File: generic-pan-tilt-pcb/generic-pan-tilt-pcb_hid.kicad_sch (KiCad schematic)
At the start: 9 parts, among them SW3 219-12LPST, U5 MCP23017_SO

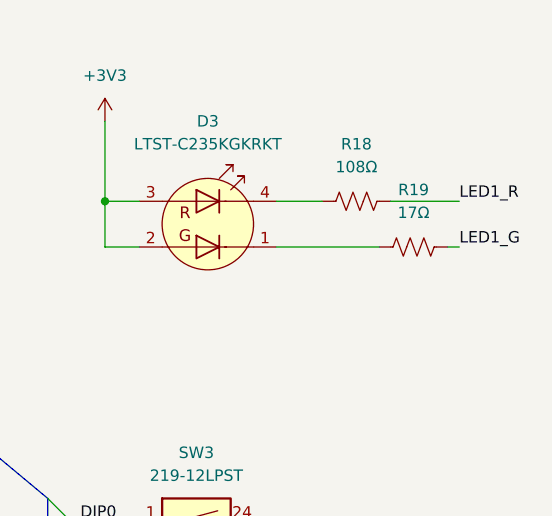
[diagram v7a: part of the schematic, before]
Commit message: fix LED resistors
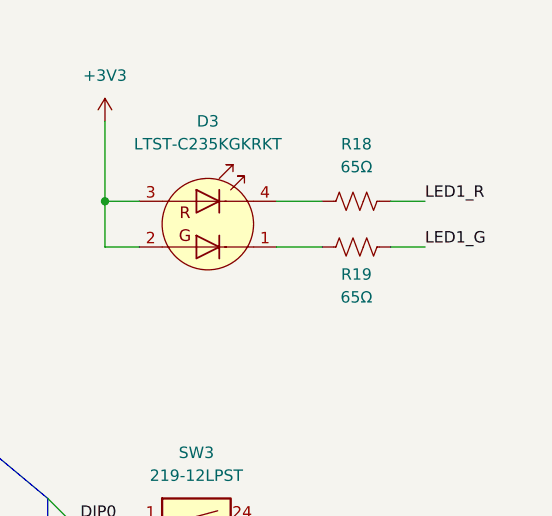
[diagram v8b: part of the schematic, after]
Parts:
- R18: value 108Ω -> 65Ω
- R19: value 17Ω -> 65Ω
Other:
- moved on the sheet: R19
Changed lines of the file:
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@@
 	(wire
 		(pts
-			(xy 232.41 59.69) (xy 233.68 59.69)
+			(xy 226.06 59.69) (xy 229.87 59.69)
 		)
 		(stroke
@@
 	(wire
 		(pts
-			(xy 213.36 59.69) (xy 224.79 59.69)
+			(xy 213.36 59.69) (xy 218.44 59.69)
 		)
 		(stroke
@@
 	(wire
 		(pts
-			(xy 226.06 54.61) (xy 233.68 54.61)
+			(xy 226.06 54.61) (xy 229.87 54.61)
 		)
 		(stroke
@@
 	)
 	(label "LED1_G"
-		(at 233.68 59.69 0)
+		(at 229.87 59.69 0)
 		(fields_autoplaced yes)
 		(effects
@@
 	)
 	(label "LED1_R"
-		(at 233.68 54.61 0)
+		(at 229.87 54.61 0)
 		(fields_autoplaced yes)
 		(effects
@@
 			)
 		)
-		(property "Value" "108Ω"
+		(property "Value" "65Ω"
 			(at 222.25 50.8 90)
 			(effects
@@
 	(symbol
 		(lib_id "Device:R_US")
-		(at 228.6 59.69 90)
+		(at 222.25 59.69 90)
 		(unit 1)
 		(exclude_from_sim no)
@@
 		(on_board yes)
 		(dnp no)
-		(fields_autoplaced yes)
 		(property "Reference" "R19"
-			(at 228.6 53.34 90)
-			(effects
-				(font
-					(size 1.27 1.27)
-				)
-			)
-		)
-		(property "Value" "17Ω"
-			(at 228.6 55.88 90)
+			(at 222.25 62.738 90)
+			(effects
+				(font
+					(size 1.27 1.27)
+				)
+			)
+		)
+		(property "Value" "65Ω"
+			(at 222.25 65.278 90)
 			(effects
 				(font
@@
 		)
 		(property "Footprint" "Capacitor_SMD:C_0402_1005Metric"
-			(at 228.854 58.674 90)
+			(at 222.504 58.674 90)
 			(effects
 				(font
@@
 		)
 		(property "Datasheet" "~"
-			(at 228.6 59.69 0)
+			(at 222.25 59.69 0)
 			(effects
 				(font
@@
 		)
 		(property "Description" "Resistor, US symbol"
-			(at 228.6 59.69 0)
-			(effects
-				(font
+			(at 222.25 59.69 0)
+			(effects
+				(font
